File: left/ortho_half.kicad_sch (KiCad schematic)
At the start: 0 parts

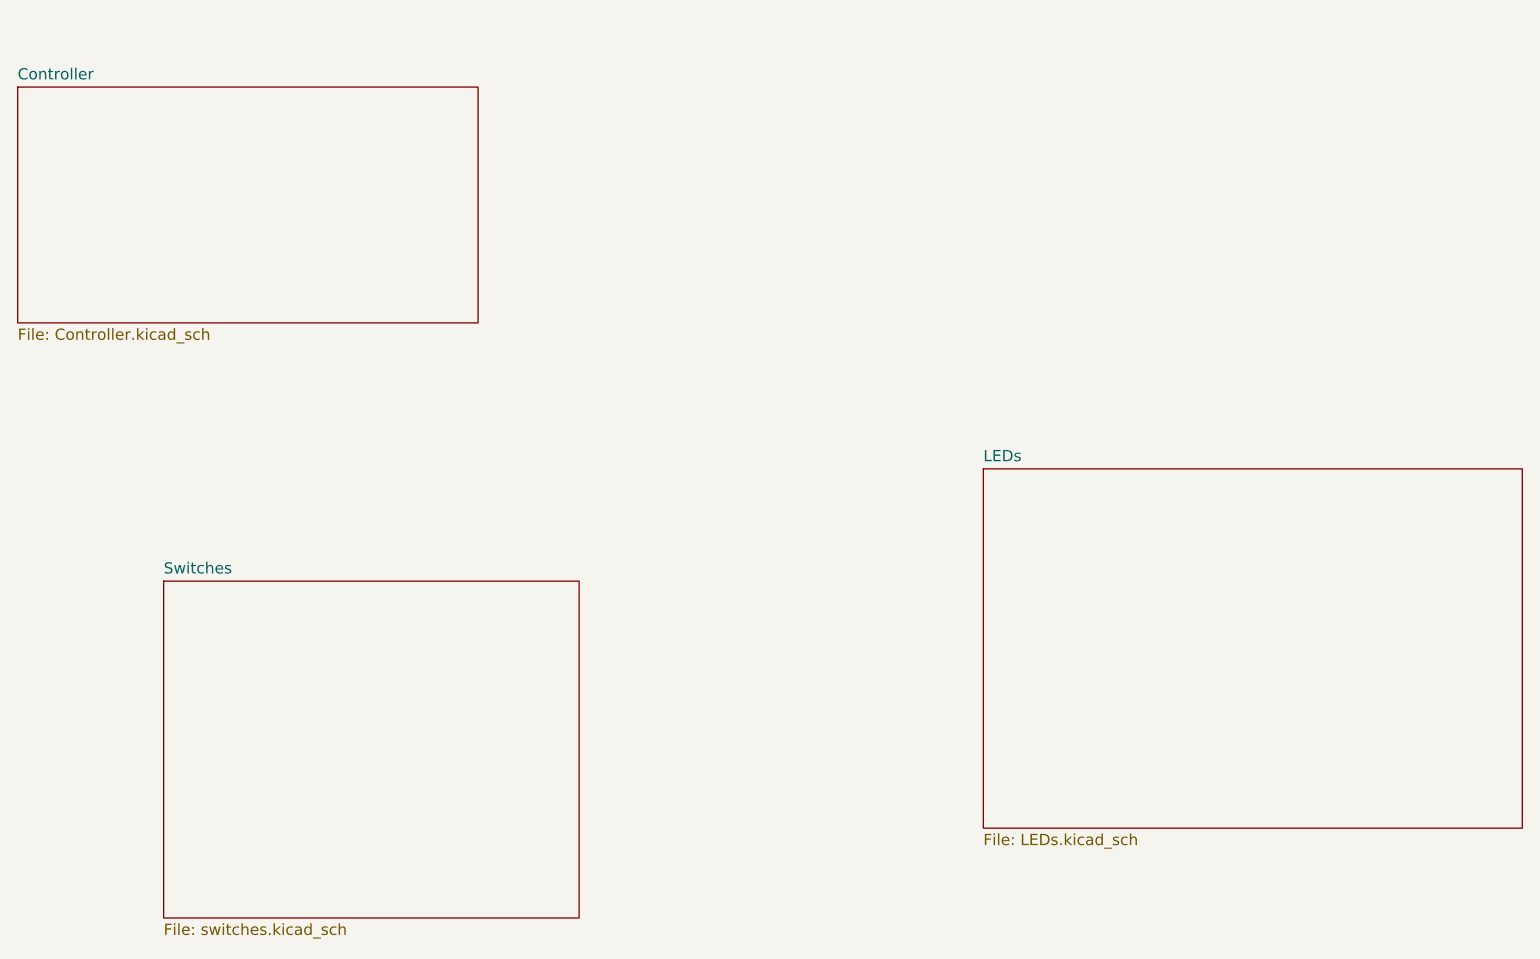
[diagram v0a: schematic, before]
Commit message: Broke out keys into individual components so that the BOM and pick and place are easier to generate.
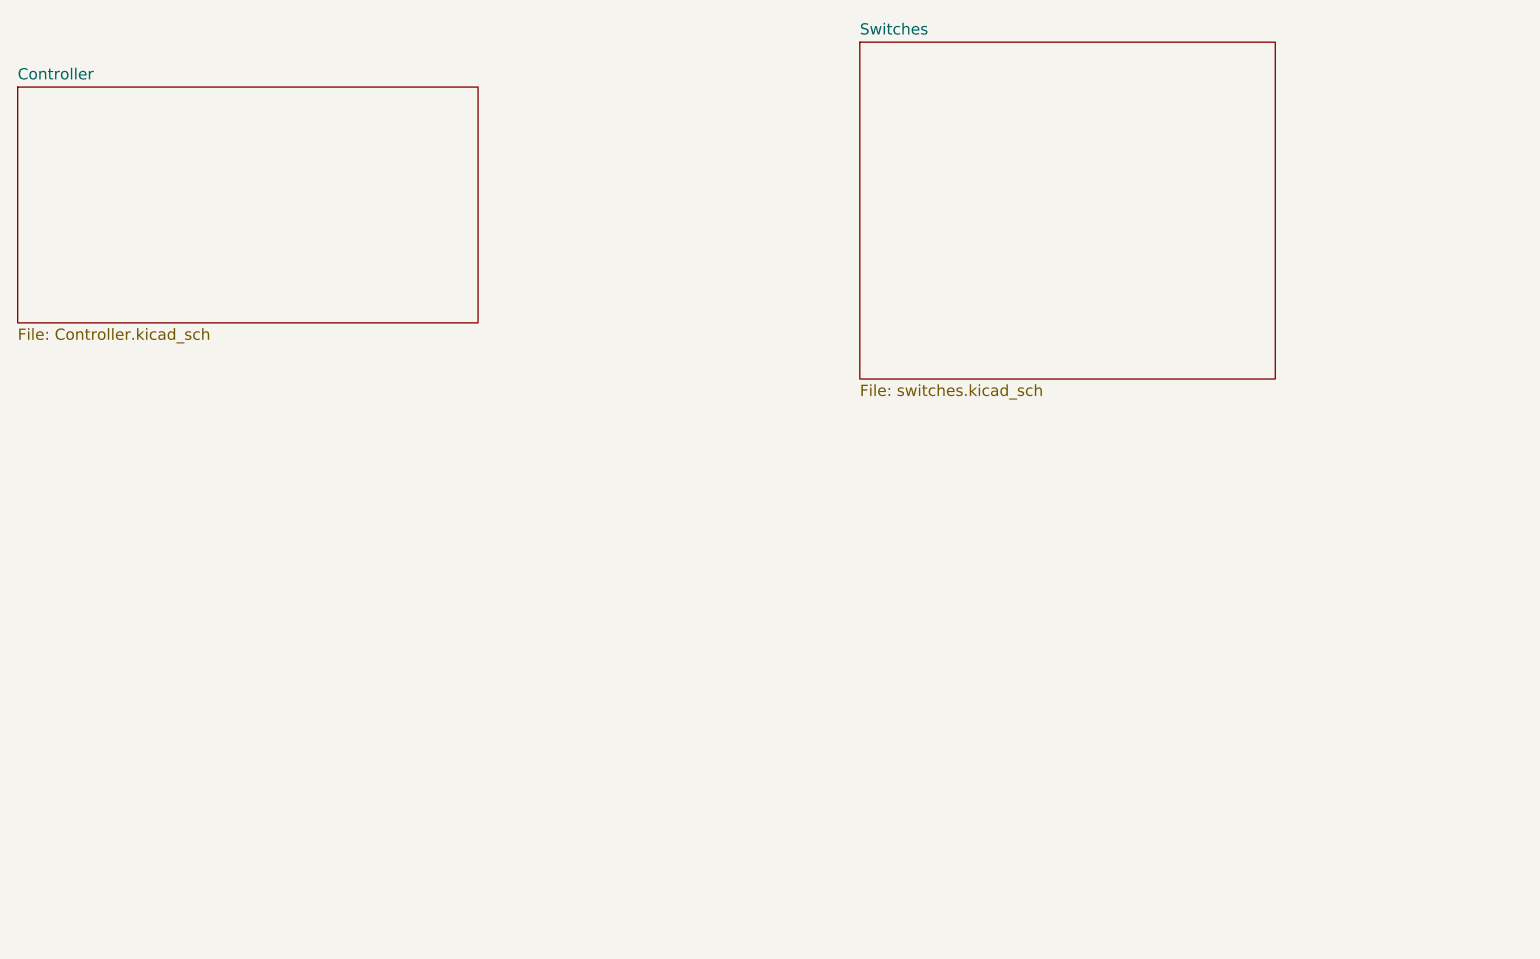
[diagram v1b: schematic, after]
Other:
- removed sheet LEDs
